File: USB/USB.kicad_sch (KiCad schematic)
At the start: 21 parts, among them J1 USBC-4-0-CX90MW9-24P1, U1 ESDA25L, U14 MUX HD3SS460RHRR, U15 USB SWITCH 2CHANNEL TS3USB221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, U16 usb-polarity-TUSB321RWBR, U3 TVS-choke-2-pair-EMI8142MUTAG, U4 TVS-choke-2-pair-EMI8142MUTAG

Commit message: add 4 layer stackup from pcbway
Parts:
- R1: footprint SPIRIT-footprints:1K-05W-0805-RES_ERJP06J102V -> SPIRIT-footprints:0805-resistor
- TVS-PUSB1: now not fitted
- renumbered C1 to C2, C66 to C5, C2 to C6, C36 to C7, R8 to R2, R9 to R3, R43 to R4, U3 to U1, U1 to U2, U15 to U3, U2 to U4, U4 to U5, U16 to U6, U14 to U7
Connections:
- net D+: no longer U3.8 (D+)
- net D+f: now also U3.8 (D+)
- net D-: no longer U3.7 (D-)
- net D-f: now also U3.7 (D-)
- net GND: now also U1.3 (GND), U1.8 (GND), U5.3 (GND), U5.8 (GND)
- net RX1+: now also U1.1 (IN_1+), U5.4 (IN_2+); no longer U7.1 (CRX1P), U7.9 (CRX2P)
- net RX1-: now also U1.2 (IN_1−), U5.5 (IN_2-); no longer U7.10 (CRX2N), U7.2 (CRX1N)
- net TX1+: now also U1.4 (IN_2+), U5.1 (IN_1+); no longer U7.4 (CTX1P), U7.6 (CTX2P)
- net TX1-: now also U1.5 (IN_2-), U5.2 (IN_1−); no longer U7.5 (CTX1N), U7.7 (CTX2N)
- net TX2+f: now reaches U5.10 (OUT_1+)
- net TX2+f: now also U7.6 (CTX2P)
- net RX2-f: now reaches U5.6 (OUT_2-)
- net RX2-f: now also U7.2 (CRX1N)
- net RX2+f: now reaches U5.7 (OUT_2+)
- net RX2+f: now also U7.1 (CRX1P)
- net TX2-f: now reaches U5.9 (OUT_1-)
- net TX2-f: now also U7.7 (CTX2N)
- net RX1+f: now reaches U1.10 (OUT_1+)
- net RX1+f: now also U7.9 (CRX2P)
- net TX1-f: now reaches U1.6 (OUT_2-)
- net TX1-f: now also U7.5 (CTX1N)
- net TX1+f: now reaches U1.7 (OUT_2+)
- net TX1+f: now also U7.4 (CTX1P)
- net RX1-f: now reaches U1.9 (OUT_1-)
- net RX1-f: now also U7.10 (CRX2N)
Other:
- note added: ""The TUSB321 device has the ability to control an external/discrete MUX using the DIR pin. The TUSB321 detects the cable orientation by monitoring the voltage on the CC pins. When a voltage level within the proper threshold is detected on CC1, the DIR pin is pulled low. When a voltage level within the proper threshold is detected on CC2, the DIR is pulled high. If the direction polarity of the ex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"
- note added: "TODO - add terminal block to power this (wago, 3V3, 5V, GND, DEBEUG?) // JUST SOLDER PADS - add patreons to silkscreen - remove unused labels - add holes in PCB for THT pins - add 'lil chamfer to indicate orientation"
- note added: "USB C TEST"
- note added: "reverse CC pins if mux is driven incorrectly (this will invert the MUX_POL signal)"
- note removed: "TEST"
- note removed: "TODO - add terminal block to power this (wago, 3V3, 5V, GND, DEBEUG?) // JUST SOLDER PADS - add patreons to silkscreen - remove unused labels - add lost TVS choke for ss signals"
- note removed: "ZD1 out of stock"
- note removed: "research pull up and open drain output"
- company: (none) -> V ELECTRONICS
- title: (none) -> USB-PROTOTYPE
- moved on the sheet: C1, C2, C3, C4, C5, C6, C7, J1, Module1A, Module1B, R2, R3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

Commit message: RX1 line problem
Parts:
- removed TVS-PUSB1: ~, SPIRIT-footprints:TVS-array-IC_PUSB3AB6Z, symbol SPIRIT-components:TVS-diode-array-PUSB3FR6
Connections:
- net RX1+f: now also U7.1 (CRX1P); no longer U7.9 (CRX2P)
- net RX1-f: now also U7.2 (CRX1N); no longer U7.10 (CRX2N)
- net RX2+f: now also U7.9 (CRX2P); no longer U7.1 (CRX1P)
- net RX2-f: now also U7.10 (CRX2N); no longer U7.2 (CRX1N)

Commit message: TVS chokes connected
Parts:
- removed U1, U5: TVS-choke-2-pair-EMI8142MUTAG, SPIRIT-footprints:2-channel-TVS-chokeXDFN10_2P2X1P3_ONS, symbol SPIRIT-components:TVS-choke-2-pair-EMI8142MUTAG
- added TVS1, TVS2: TVS-choke-2-pair-EMI8142MUTAG, SPIRIT-footprints:2-channel-TVS-chokeXDFN10_2P2X1P3_ONS, symbol SPIRIT-components:TVS-choke-2-pair-EMI8142MUTAG
- renumbered U7 to MUX1, U4 to TVS3
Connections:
- net GND: now also TVS1.3 (GND), TVS1.8 (GND), TVS2.3 (GND), TVS2.8 (GND)
- net RX1+: now also TVS1.1 (IN_1+); no longer C2.2, J1.A11 (RX2+)
- net RX1+f: now also TVS1.10 (OUT_1+)
- net RX1-: now also TVS1.2 (IN_1−); no longer C1.2, J1.A10 (RX2-)
- net RX1-f: now also TVS1.9 (OUT_1-)
- net RX2+f: now also TVS2.7 (OUT_2+)
- net RX2-f: now also TVS2.6 (OUT_2-)
- net SSTR2+: now also C2.2
- net SSTR2-: now also C1.2
- net SSTX2+: now also C4.2
- net SSTX2-: now also C3.2
- net TX1+: now also TVS1.4 (IN_2+); no longer C4.2, J1.B2 (TX2+)
- net TX1+f: now also TVS1.7 (OUT_2+)
- net TX1-: now also TVS1.5 (IN_2-); no longer C3.2, J1.B3 (TX2-)
- net TX1-f: now also TVS1.6 (OUT_2-)
- net TX2+f: now also TVS2.10 (OUT_1+)
- net TX2-f: now also TVS2.9 (OUT_1-)
- new net RX2+: J1.A11 (RX2+), TVS2.4 (IN_2+)
- new net RX2-: J1.A10 (RX2-), TVS2.5 (IN_2-)
- new net TX2+: J1.B2 (TX2+), TVS2.1 (IN_1+)
- new net TX2-: J1.B3 (TX2-), TVS2.2 (IN_1−)

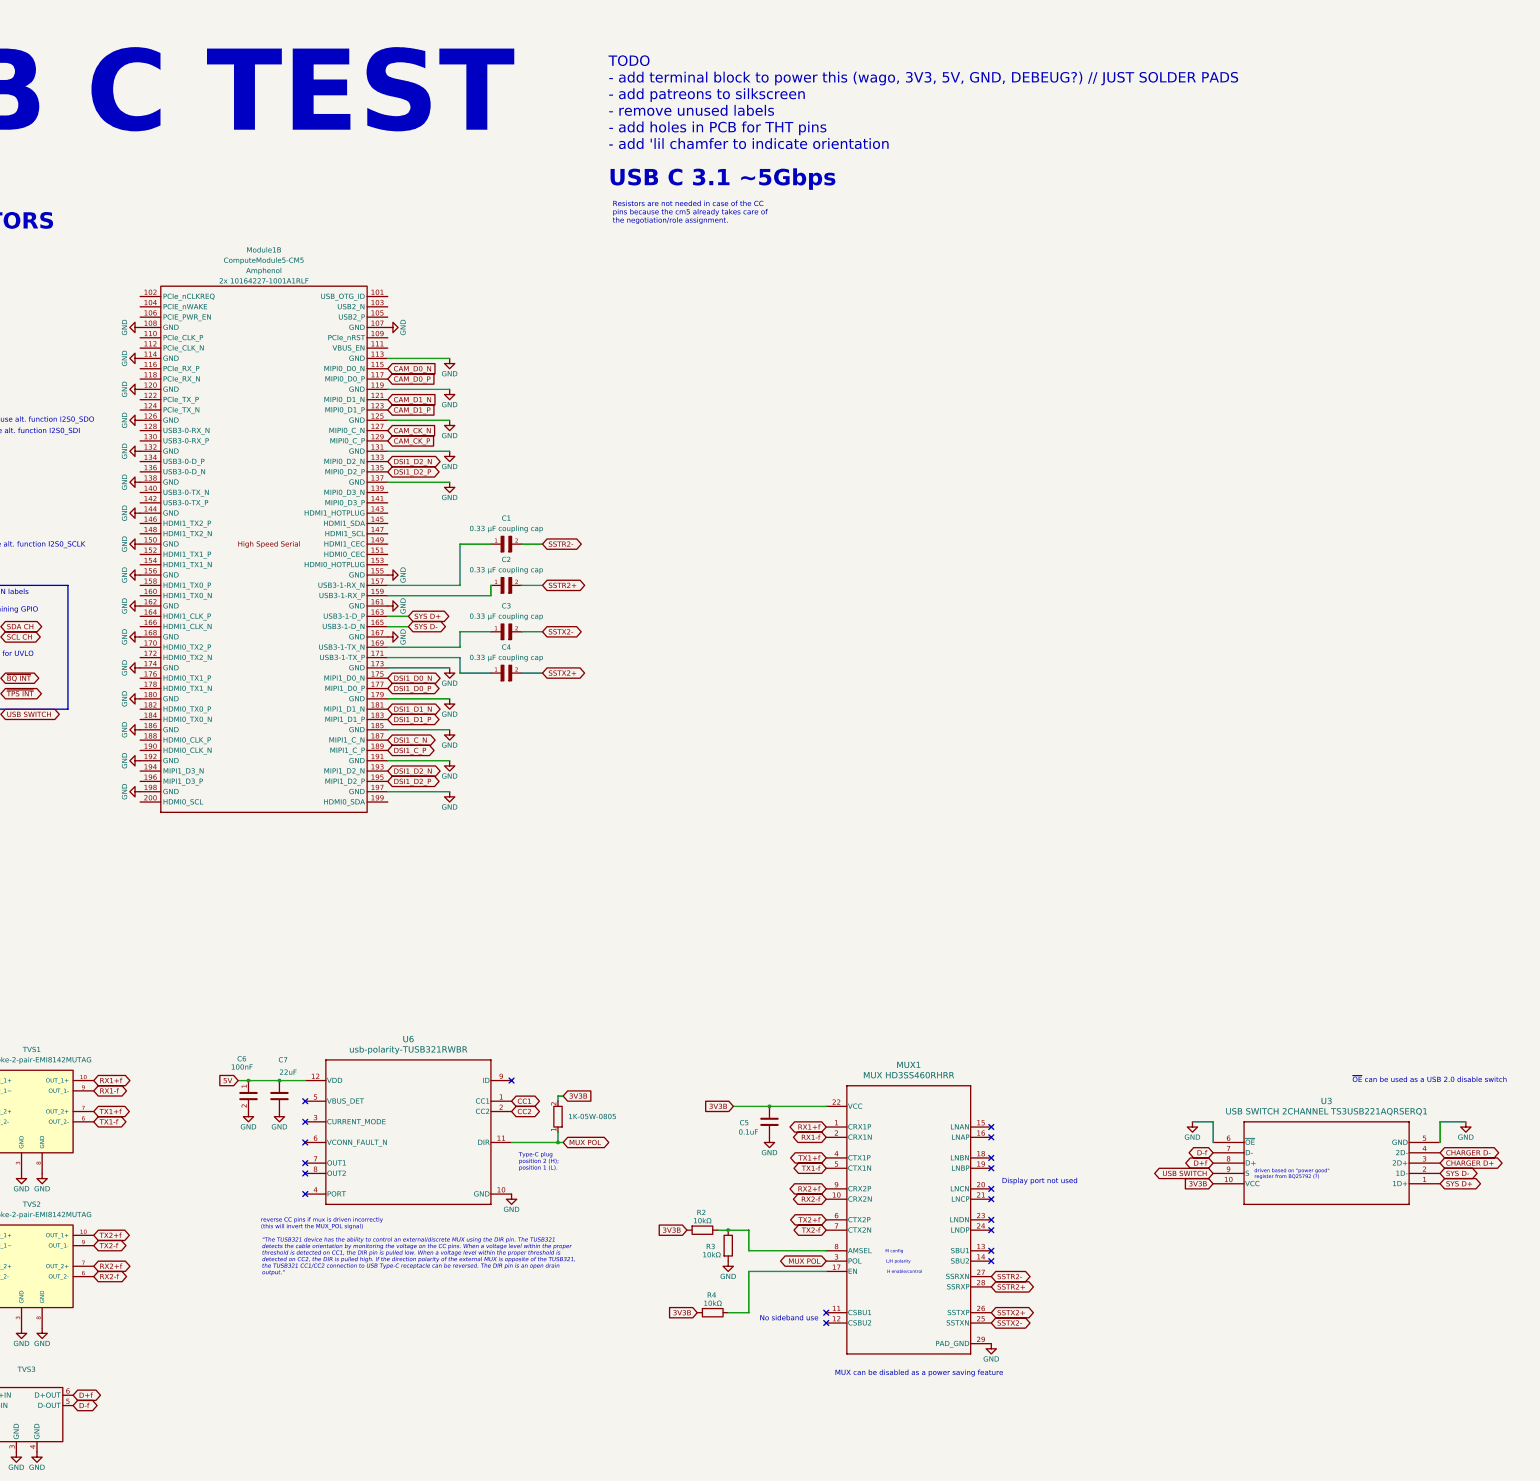
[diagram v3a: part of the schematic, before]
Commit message: reroute data lines for Zd
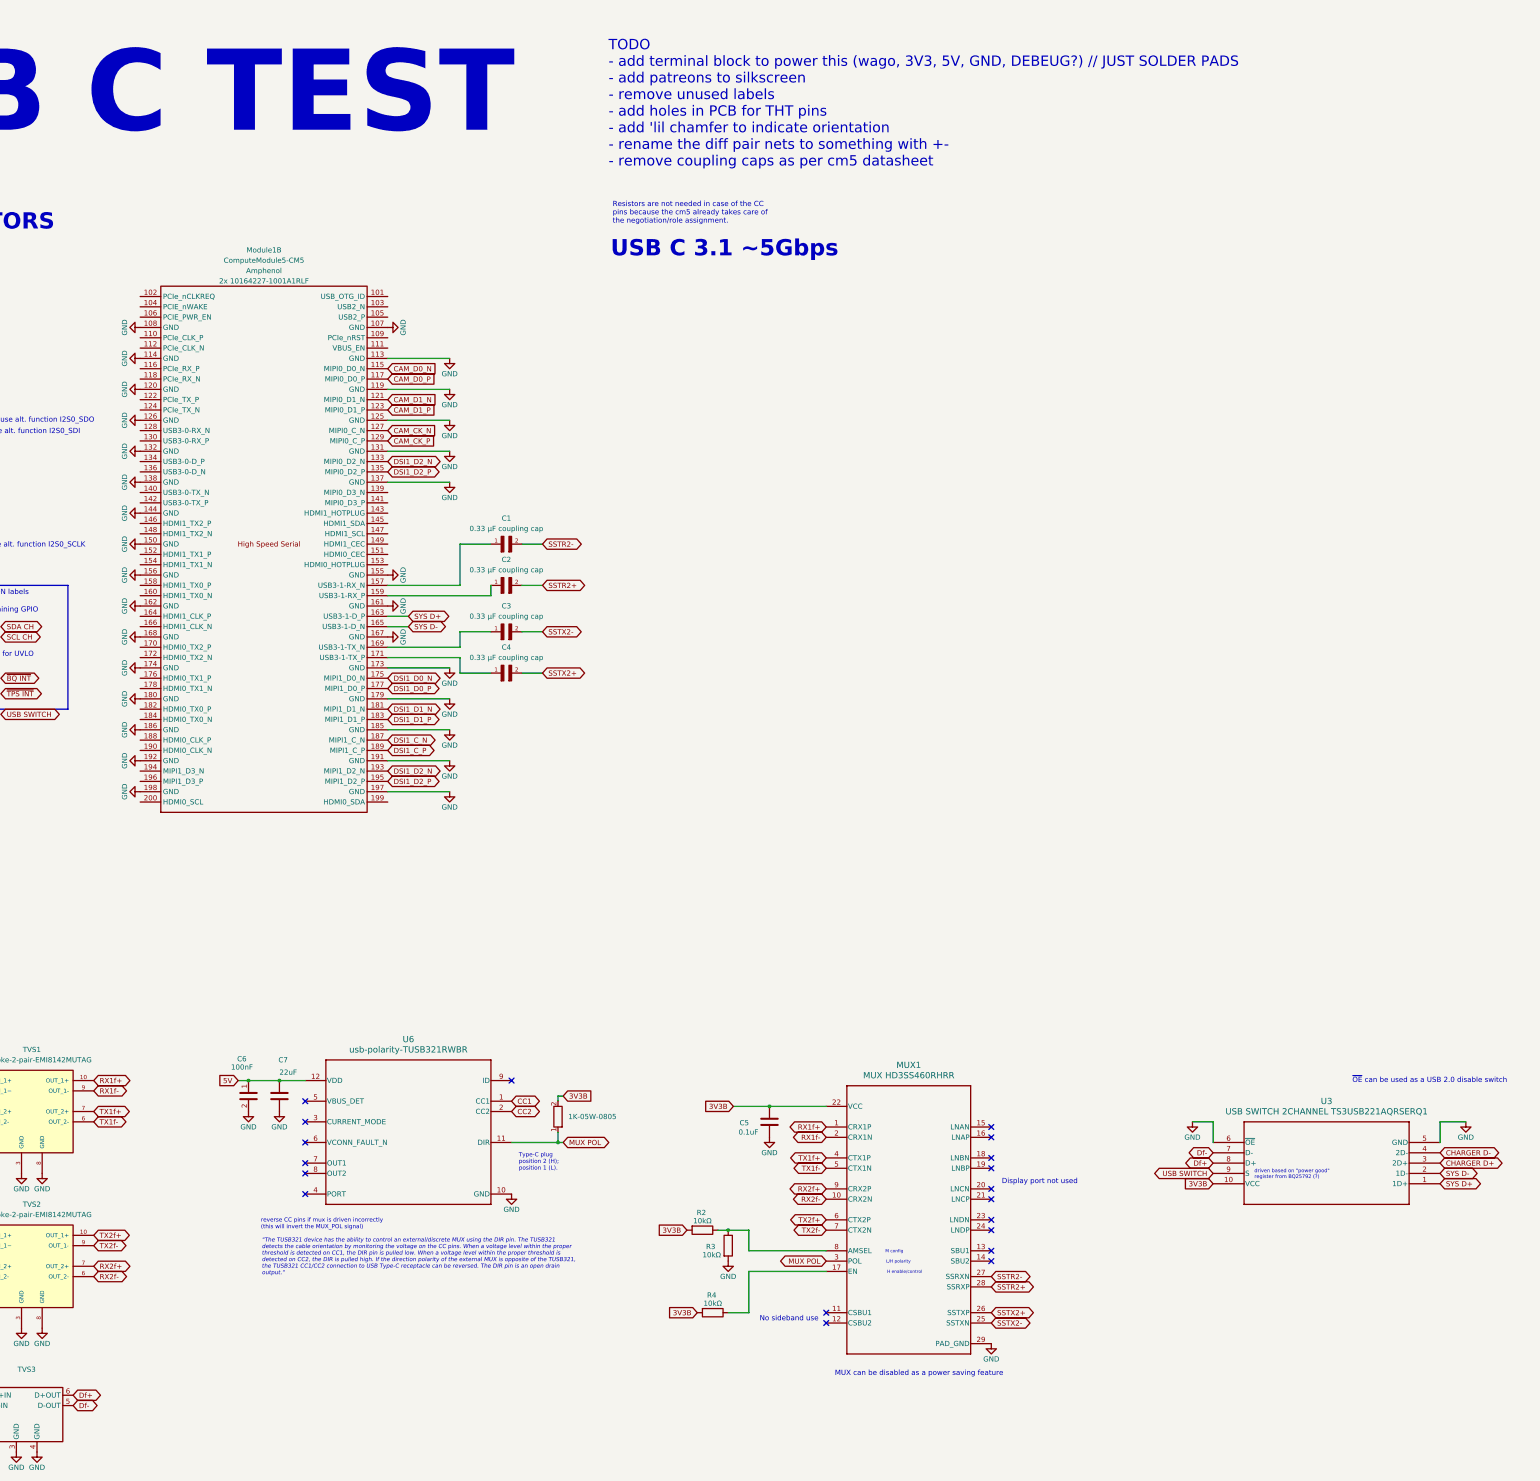
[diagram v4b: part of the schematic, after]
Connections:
- net D+f renamed Df+
- net D-f renamed Df-
- net RX1+f renamed RX1f+
- net RX1-f renamed RX1f-
- net RX2+f renamed RX2f+
- net RX2-f renamed RX2f-
- net TX1+f renamed TX1f+
- net TX1-f renamed TX1f-
- net TX2+f renamed TX2f+
- net TX2-f renamed TX2f-
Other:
- note added: "TODO - add terminal block to power this (wago, 3V3, 5V, GND, DEBEUG?) // JUST SOLDER PADS - add patreons to silkscreen - remove unused labels - add holes in PCB for THT pins - add 'lil chamfer to indicate orientation - rename the diff pair nets to something with +- - remove coupling caps as per cm5 datasheet"
- note removed: "TODO - add terminal block to power this (wago, 3V3, 5V, GND, DEBEUG?) // JUST SOLDER PADS - add patreons to silkscreen - remove unused labels - add holes in PCB for THT pins - add 'lil chamfer to indicate orientation"

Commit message: progress
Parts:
- removed C1, C2, C3, C4: 0.33 µF coupling cap, SPIRIT-footprints:USBC_capacitor_CAPC0603X33N, symbol SPIRIT-components:USBC_capacitor_GRM033R60J334ME90D
- added J2, J3: ~, Connector_PinHeader_1.00mm:PinHeader_1x02_P1.00mm_Vertical, symbol SPIRIT-components:2-pin-header
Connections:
- net CC1: now also J2.1; no longer U6.1 (CC1)
- net CC2: now also J3.1; no longer U6.2 (CC2)
- net GND: no longer J1.A1 (GND_A), J1.A12 (GND_A__1)
- net SSTR2+: now also Module1.159 (USB3-1-RX_P)
- net SSTR2-: now also Module1.157 (USB3-1-RX_N)
- net SSTX2+: now also Module1.171 (USB3-1-TX_P)
- net SSTX2-: now also Module1.169 (USB3-1-TX_N)
- new net: J2.2, U6.1 (CC1)
- new net: J3.2, U6.2 (CC2)
- new net: J1.A1 (GND_A), J1.A12 (GND_A__1)
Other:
- note added: "TODO - add terminal block to power this (wago, 3V3, 5V, GND, DEBEUG?) // JUST SOLDER PADS - add patreons to silkscreen - remove unused labels x- add pin header symbol for polarity flipper x- add 'lil chamfer to indicate orientation x- rename the diff pair nets to something with +- x- remove coupling caps as per cm5 datasheet"
- note removed: "TODO - add terminal block to power this (wago, 3V3, 5V, GND, DEBEUG?) // JUST SOLDER PADS - add patreons to silkscreen - remove unused labels - add holes in PCB for THT pins - add 'lil chamfer to indicate orientation - rename the diff pair nets to something with +- - remove coupling caps as per cm5 datasheet"

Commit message: update to kicad 10
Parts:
- J2, J3, TVS3: value ~ -> (none)
